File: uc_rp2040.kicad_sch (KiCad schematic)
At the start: 35 parts

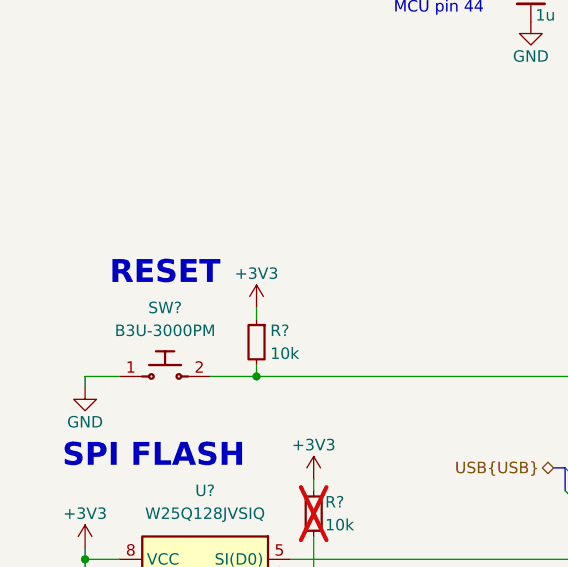
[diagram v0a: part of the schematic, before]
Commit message: [#72133] Add USB mux
Signed-off-by: Dawid Lentka <dlentka@antmicro.com>
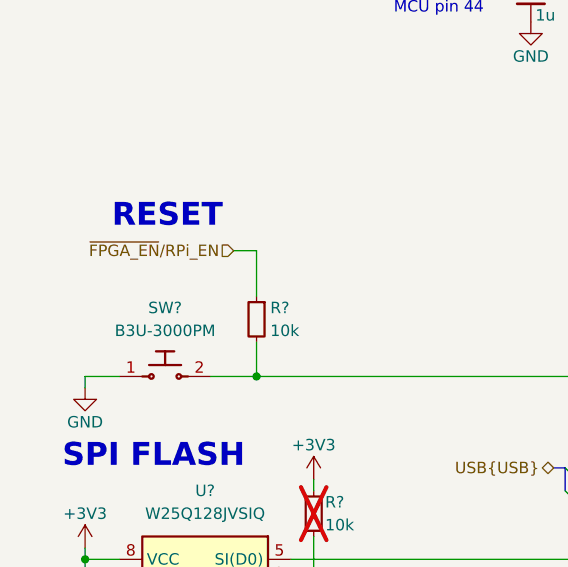
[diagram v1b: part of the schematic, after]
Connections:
- net +3V3: no longer R?.1
- new net ~{FPGA_EN}/RPi_EN: R?.1
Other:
- moved on the sheet: R?
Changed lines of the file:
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@@
 	(wire
 		(pts
-			(xy 91.44 95.25) (xy 91.44 96.52)
+			(xy 91.44 92.71) (xy 91.44 96.52)
 		)
 		(stroke
@@
 	(wire
 		(pts
+			(xy 88.9 82.55) (xy 91.44 82.55)
+		)
+		(stroke
+			(width 0)
+			(type default)
+		)
+	)
+	(wire
+		(pts
 			(xy 121.92 50.8) (xy 128.27 50.8)
 		)
@@
 	(wire
 		(pts
-			(xy 91.44 88.9) (xy 91.44 90.17)
-		)
-		(stroke
-			(width 0)
-			(type default)
-		)
-	)
-	(wire
-		(pts
 			(xy 199.39 144.78) (xy 231.14 144.78)
 		)
@@
 	(wire
 		(pts
+			(xy 91.44 82.55) (xy 91.44 87.63)
+		)
+		(stroke
+			(width 0)
+			(type default)
+		)
+	)
+	(wire
+		(pts
 			(xy 99.06 129.54) (xy 99.06 134.62)
 		)
@@
 	(text "RESET"
 		(exclude_from_sim no)
-		(at 81.28 85.09 0)
+		(at 81.534 78.74 0)
 		(effects
 			(font
@@
 		)
 	)
+	(hierarchical_label "~{FPGA_EN}{slash}RPi_EN"
+		(shape input)
+		(at 88.9 82.55 180)
+		(fields_autoplaced yes)
+		(effects
+			(font
+				(size 1.27 1.27)
+			)
+			(justify right)
+		)
+	)
 	(hierarchical_label "Trig{Triggers}"
 		(shape input)
@@
 	(symbol
 		(lib_id "antmicroResistors0402:R_10k_0402")
-		(at 91.44 90.17 270)
+		(at 91.44 87.63 270)
 		(unit 1)
 		(exclude_from_sim no)
@@
 		(dnp no)
 		(property "Reference" "R?"
-			(at 92.964 91.44 90)
+			(at 92.964 88.9 90)
 			(effects
 				(font
@@
 		)
 		(property "Value" "R_10k_0402"
-			(at 78.74 110.49 0)
+			(at 78.74 107.95 0)
 			(effects
 				(font
@@
 		)
 		(property "Footprint" "antmicro-footprints:R_0402_1005Metric"
-			(at 76.2 110.49 0)
+			(at 76.2 107.95 0)
 			(effects
 				(font
@@
 		)
 		(property "Datasheet" "https://www.bourns.com/docs/product-datasheets/cr.pdf"
-			(at 73.66 110.49 0)
+			(at 73.66 107.95 0)
 			(effects
 				(font
@@
 		)
 		(property "Description" "SMD Chip Resistor, 10 kohm, ± 1%, 62.5 mW, 0402 [1005 Metric], Thick Film, General Purpose"
-			(at 91.44 90.17 0)
+			(at 91.44 87.63 0)
 			(effects
 				(font
@@
 		)
 		(property "MPN" "CR0402-FX-1002GLF"
-			(at 71.12 110.49 0)
+			(at 71.12 107.95 0)
 			(effects
 				(font
@@
 		)
 		(property "Manufacturer" "Bourns"
-			(at 68.58 110.49 0)
+			(at 68.58 107.95 0)
 			(effects
 				(font
@@
 		)
 		(property "License" "Apache-2.0"
-			(at 66.04 110.49 0)
+			(at 66.04 107.95 0)
 			(effects
 				(font
@@
 		)
 		(property "Author" "Antmicro"
-			(at 63.5 110.49 0)
+			(at 63.5 107.95 0)
 			(effects
 				(font
@@
 		)
 		(property "Val" "10k"
-			(at 92.964 93.98 90)
+			(at 92.964 91.44 90)
 			(effects
 				(font
@@
 		)
 		(property "Tolerance" "1%"
-			(at 81.28 110.49 0)
+			(at 81.28 107.95 0)
 			(effects
 				(font
@@
 					(unit 1)
 				)
-			)
-		)
-	)
-	(symbol
-		(lib_id "antmicropower:+3V3")
-		(at 91.44 88.9 0)
-		(unit 1)
-		(exclude_from_sim no)
-		(in_bom yes)
-		(on_board yes)
-		(dnp no)
-		(property "Reference" "#PWR057"
-			(at 106.68 88.9 0)
-			(effects
-				(font
-					(size 1.27 1.27)
-					(thickness 0.15)
-				)
-				(justify left bottom)
-				(hide yes)
-			)
-		)
-		(property "Value" "+3V3"
-			(at 91.44 85.09 0)
-			(effects
-				(font
-					(size 1.27 1.27)
-					(thickness 0.15)
-				)
-			)
-		)
-		(property "Footprint" ""
-			(at 106.68 96.52 0)
-			(effects
-				(font
-					(size 1.27 1.27)
-					(thickness 0.15)
-				)
-				(justify left bottom)
-				(hide yes)
-			)
-		)
-		(property "Datasheet" ""
-			(at 106.68 99.06 0)
-			(effects
-				(font
-					(size 1.27 1.27)
-					(thickness 0.15)
-				)
-				(justify left bottom)
-				(hide yes)
-			)
-		)
-		(property "Description" ""
-			(at 91.44 88.9 0)
-			(effects
-				(font
-					(size 1.27 1.27)
-				)
-				(hide yes)
-			)
-		)
-		(property "Author" "Antmicro"
-			(at 106.68 91.44 0)
-			(effects
-				(font
-					(size 1.27 1.27)
-					(thickness 0.15)
-				)
-				(justify left bottom)
-				(hide yes)
-			)
-		)
-		(property "License" "Apache-2.0"
-			(at 106.68 93.98 0)
-			(effects
-				(font
-					(size 1.27 1.27)
-					(thickness 0.15)
-				)
-				(justify left bottom)
-				(hide yes)
-			)
-		)
-		(pin "1"
-		)
-		(instances
-			(project "led-panel"
-				(path "/a86e1cab-ea0a-45e6-9194-d44b0d5c9450/06971436-f55c-4c9a-b2a5-5e1b832e9517"
-					(reference "#PWR057")
-					(unit 1)
-				)

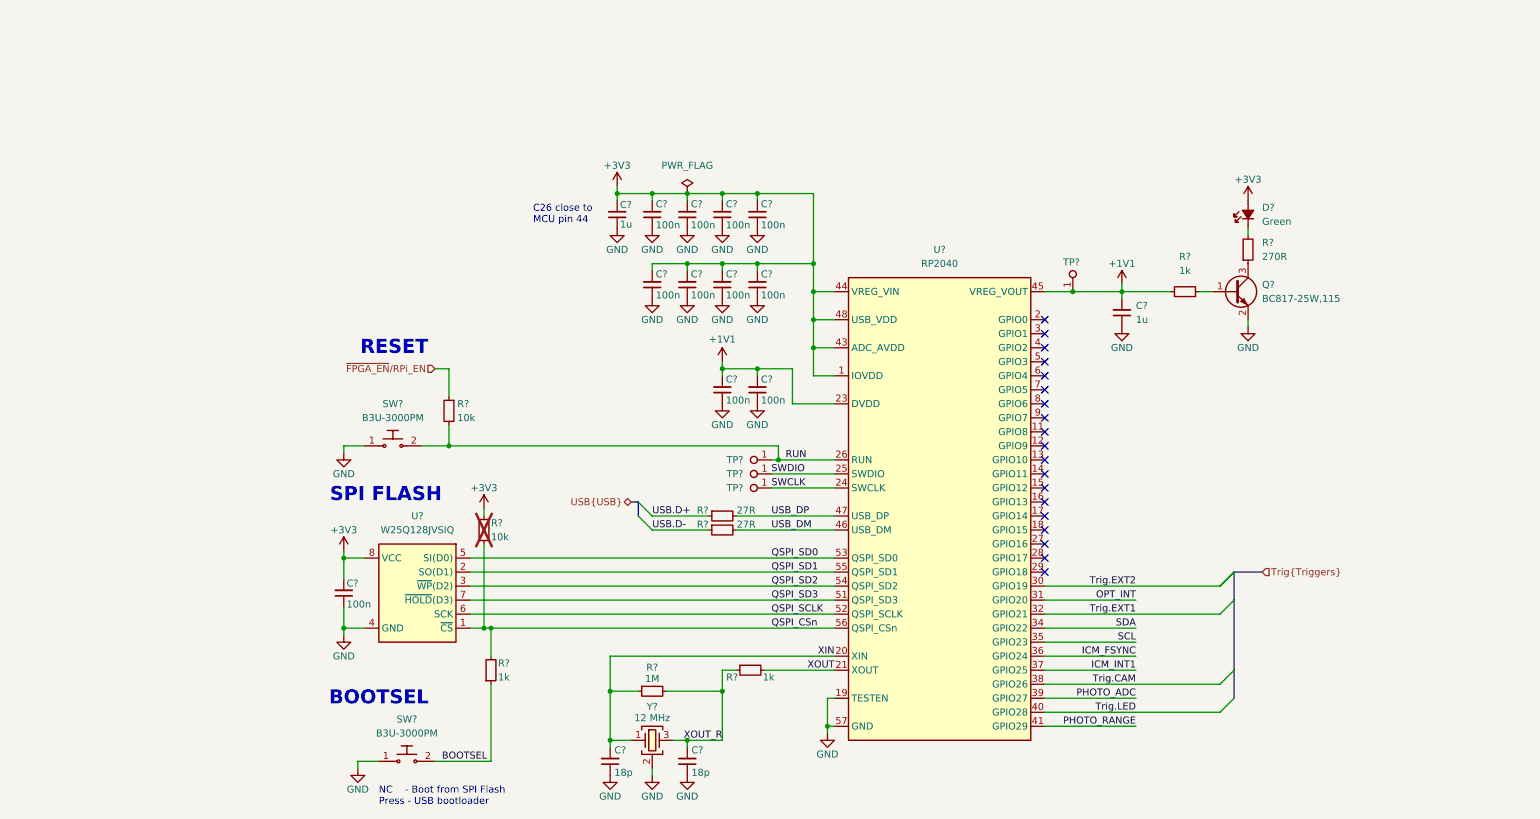
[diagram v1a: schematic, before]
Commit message: [#72133] Move executor switching to new scheet; Add FPGA flash programmer
Signed-off-by: Dawid Lentka <dlentka@antmicro.com>
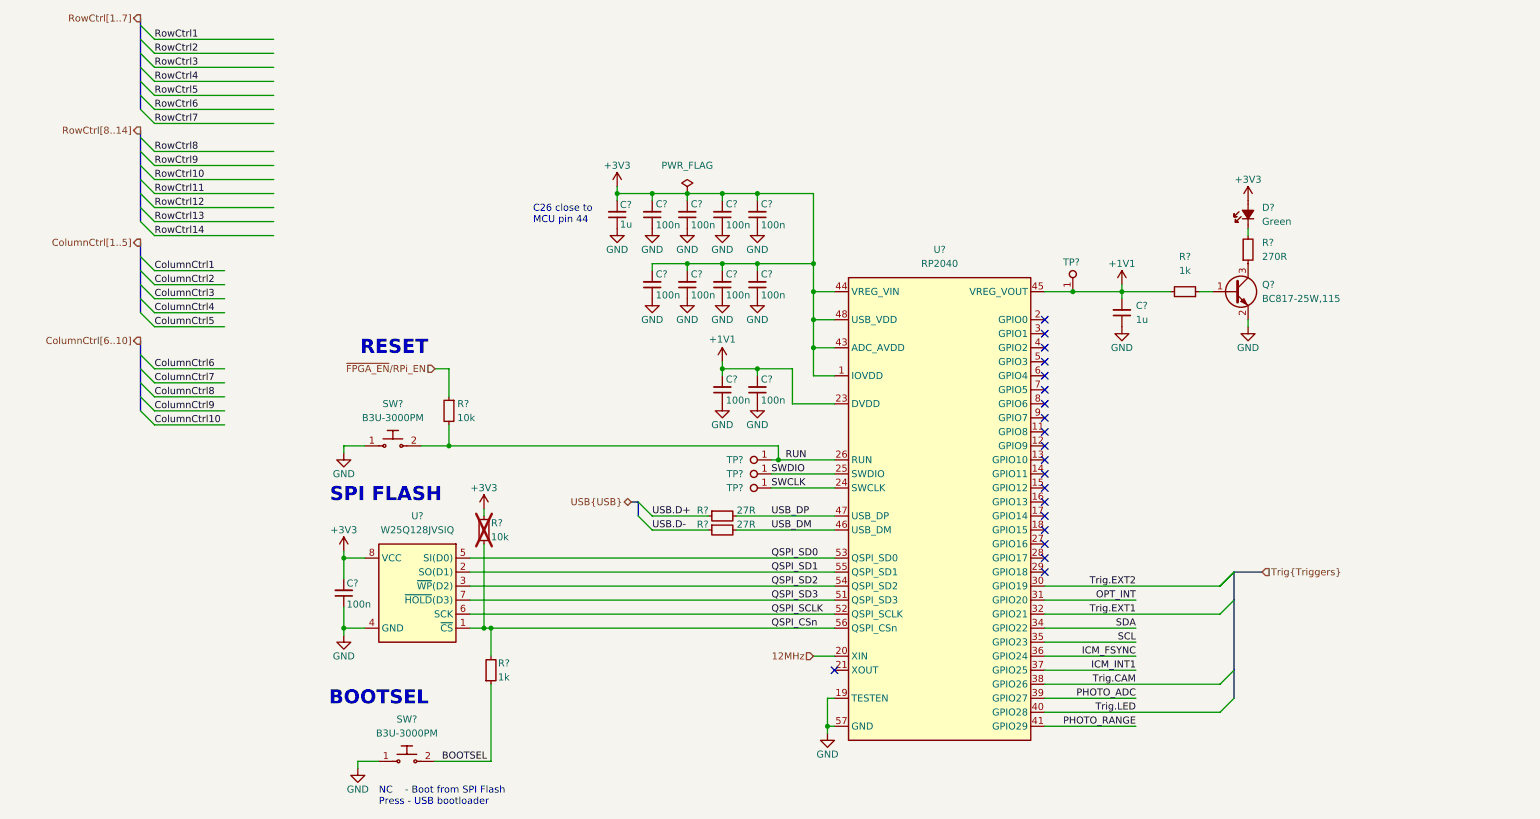
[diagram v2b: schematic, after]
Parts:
- removed C? (x2): C_18p_0402, antmicro-footprints:C_0402_1005Metric, symbol antmicroCapacitors0402:C_18p_0402
- removed R?: R_1k_0402, antmicro-footprints:R_0402_1005Metric, symbol antmicroResistors0402:R_1k_0402
- removed R?: R_1M_0402, antmicro-footprints:R_0402_1005Metric, symbol antmicroResistors0402:R_1M_0402
- removed Y?: Resonator_12MHz_ABM8G, antmicro-footprints:Resonator_SMD_Abracon_ABM8G_3.2x2.5mm, symbol antmicroResonators:Resonator_12MHz_ABM8G
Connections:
- net XIN renamed 12MHz
- net XOUT: no longer names the net of U?.21 (XOUT)
- no-connect marks 19 -> 20

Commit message: [#72133] Unify sheet size
Signed-off-by: Dawid Lentka <dlentka@antmicro.com>
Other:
- title: (none) -> LED Panel Board
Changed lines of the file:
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@@
 	(generator_version "8.0")
 	(paper "A4")
+	(title_block
+		(title "LED Panel Board")
+		(date "28.01.2025")
+		(rev "1.0.0")
+	)
 	(bus_alias "LEDCtrl"
 		(members "Row[1..14]" "Column[1..7]")

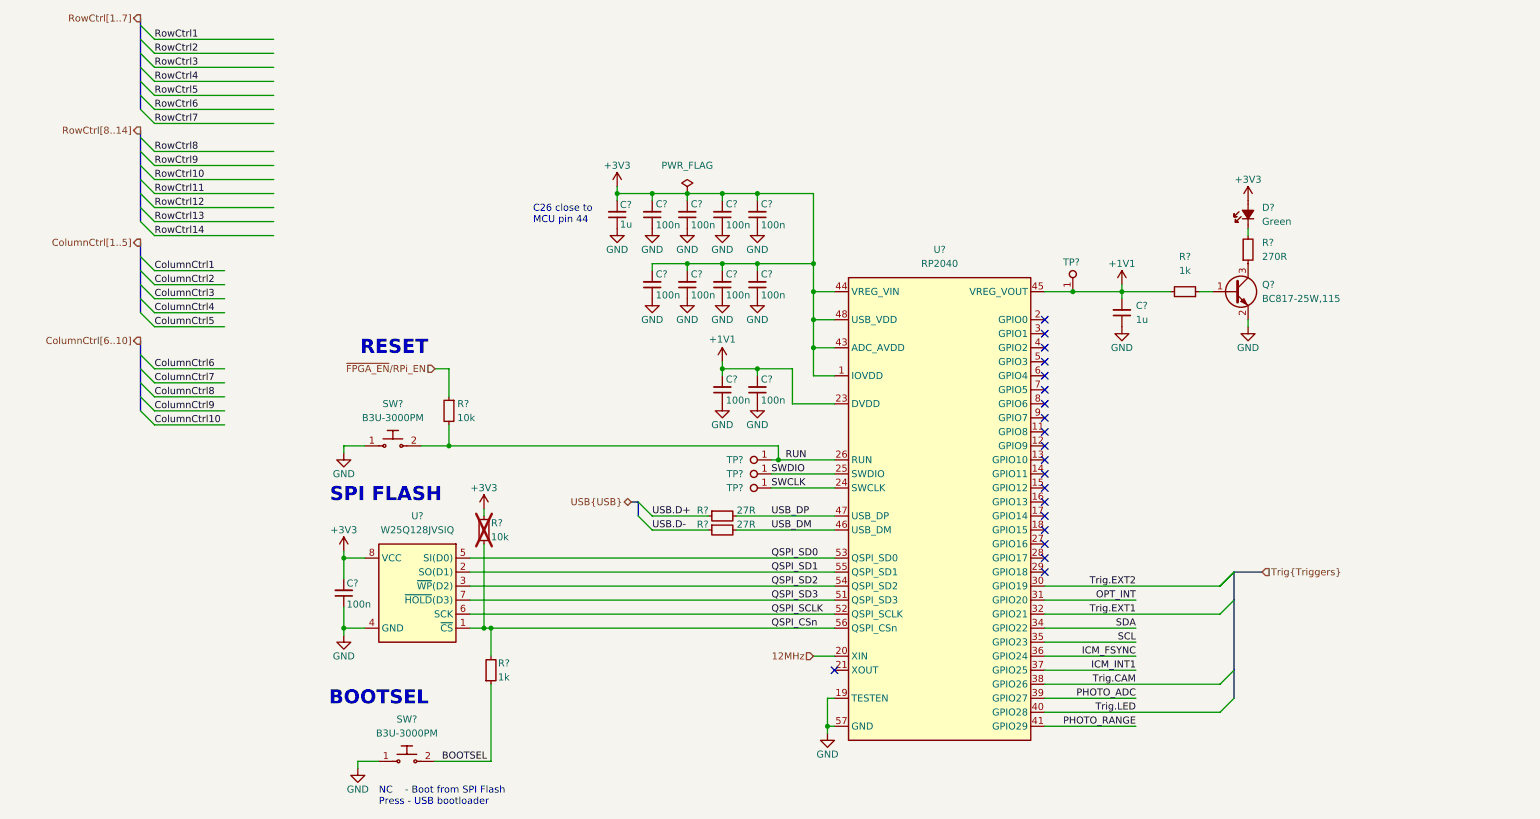
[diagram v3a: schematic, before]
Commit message: [#72133] Add indicator LEDs & testpoints
Signed-off-by: Dawid Lentka <dlentka@antmicro.com>
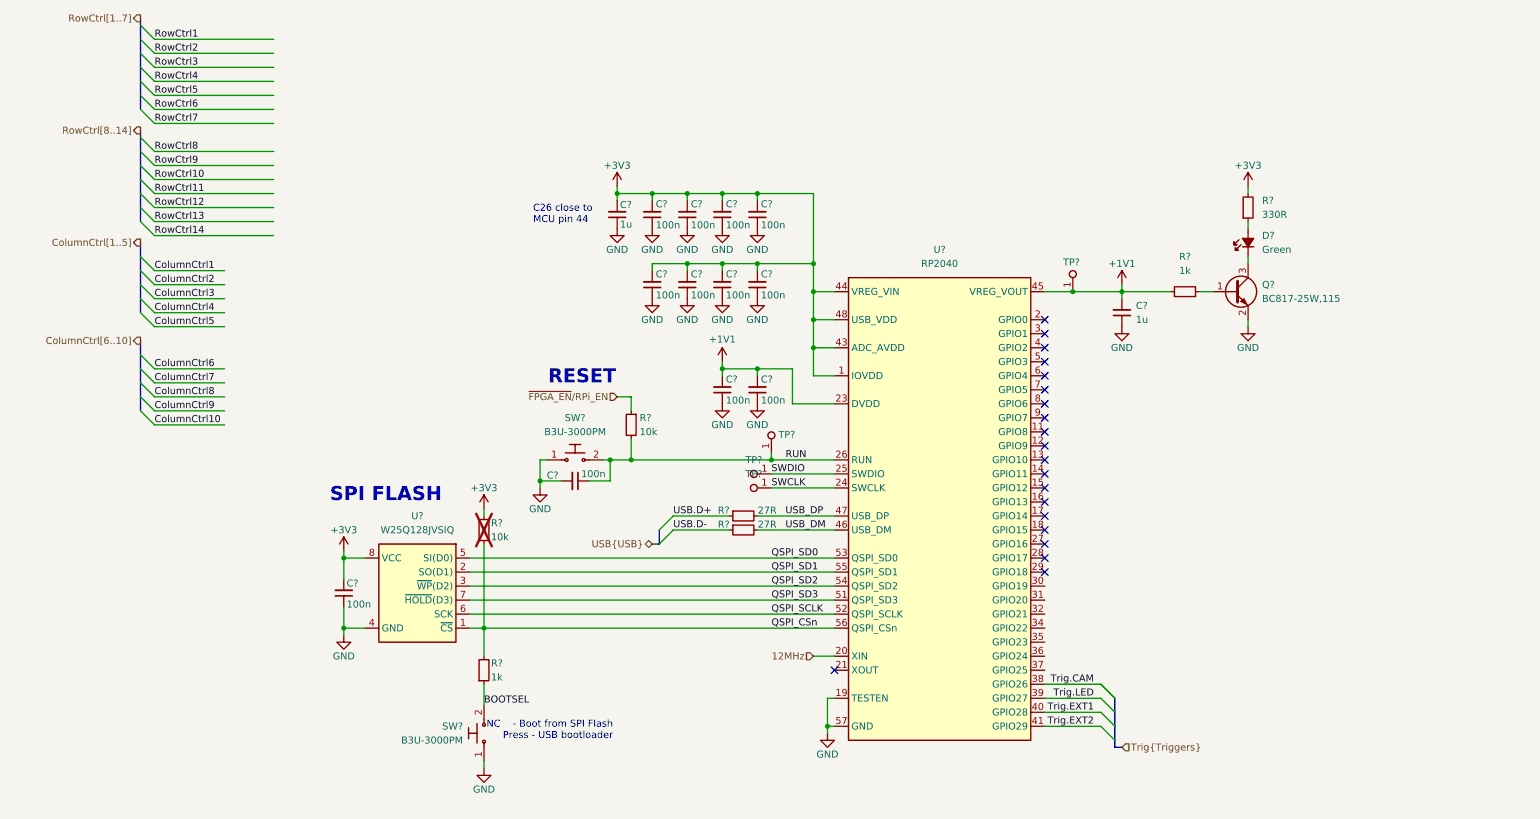
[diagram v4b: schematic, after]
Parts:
- removed D?: LED_G_0402_VLMTG1500-GS08, antmicro-footprints:LED_0402_1005Metric_G, symbol antmicroLEDIndicationDiscrete:LED_G_0402_VLMTG1500-GS08
- removed R?: R_270R_0402, antmicro-footprints:R_0402_1005Metric, symbol antmicroResistors0402:R_270R_0402
- added C?: C_100n_16V_X7R_0402, antmicro-footprints:C_0402_1005Metric, symbol antmicroCapacitors0402:C_100n_16V_X7R_0402
- added D?: LED_G_0603_KP-1608CGCK, antmicro-footprints:LED_0603_1608Metric_G, symbol antmicroLEDIndicationDiscrete:LED_G_0603_KP-1608CGCK
- added R?: R_330R_0402, antmicro-footprints:R_0402_1005Metric, symbol antmicroResistors0402:R_330R_0402
- TP? (x4): value TP_1mm_SMD -> TP_0.75mm_SMD; footprint antmicro-footprints:TP_SMD_1mm -> antmicro-footprints:TP_SMD_0.75mm; symbol antmicroTestPoints:TP_1mm_SMD -> antmicroTestPoints:TP_0.75mm_SMD
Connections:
- net PHOTO_ADC is gone; now on net Trig.LED: U?.39 (GPIO27)
- net PHOTO_RANGE is gone; now on net Trig.EXT2: U?.41 (GPIO29)
- net +3V3: now also R?.2
- net GND: now also C?.2
- net RUN: now also C?.1
- net Trig.EXT1: now also U?.40 (GPIO28); no longer U?.32 (GPIO21)
- net Trig.EXT2: no longer U?.30 (GPIO19)
- net Trig.LED: no longer U?.40 (GPIO28)
- net at Q?.3 (C): now also D?.1 (C)
- net ICM_FSYNC: no longer names the net of U?.36 (GPIO24)
- net ICM_INT1: no longer names the net of U?.37 (GPIO25)
- net OPT_INT: no longer names the net of U?.31 (GPIO20)
- net SCL: no longer names the net of U?.35 (GPIO23)
- net SDA: no longer names the net of U?.34 (GPIO22)
- new net: D?.2 (A), R?.1
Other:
- note removed: "BOOTSEL"
- moved on the sheet: R?, SW?, TP?

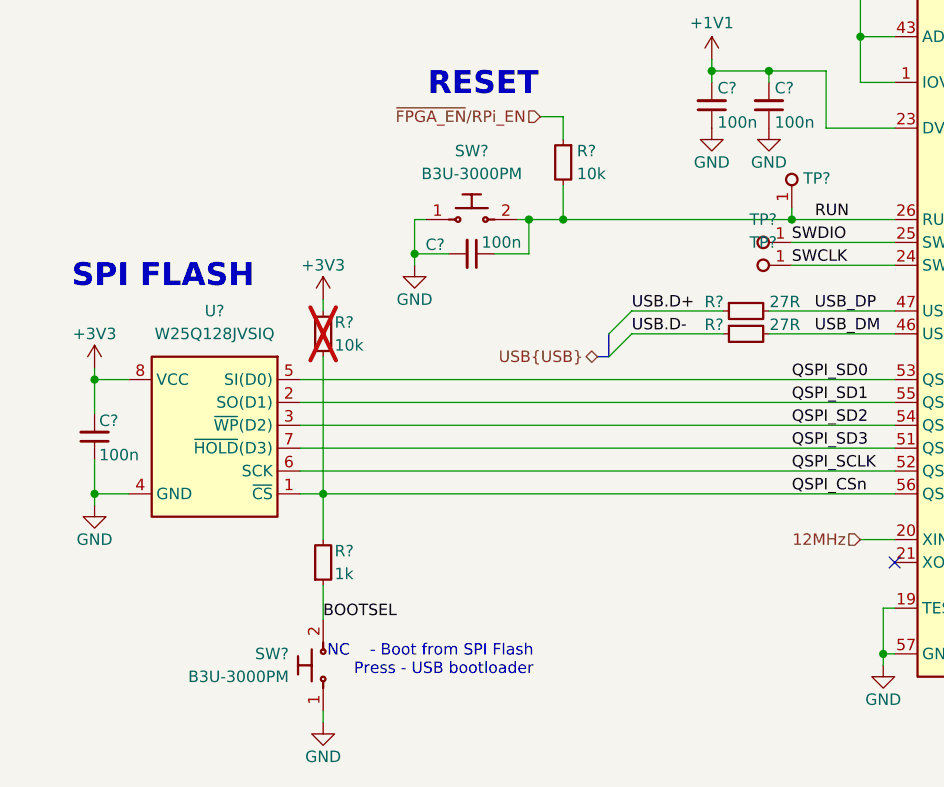
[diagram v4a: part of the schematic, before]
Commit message: [#72133] Unify components
Signed-off-by: Dawid Lentka <dlentka@antmicro.com>
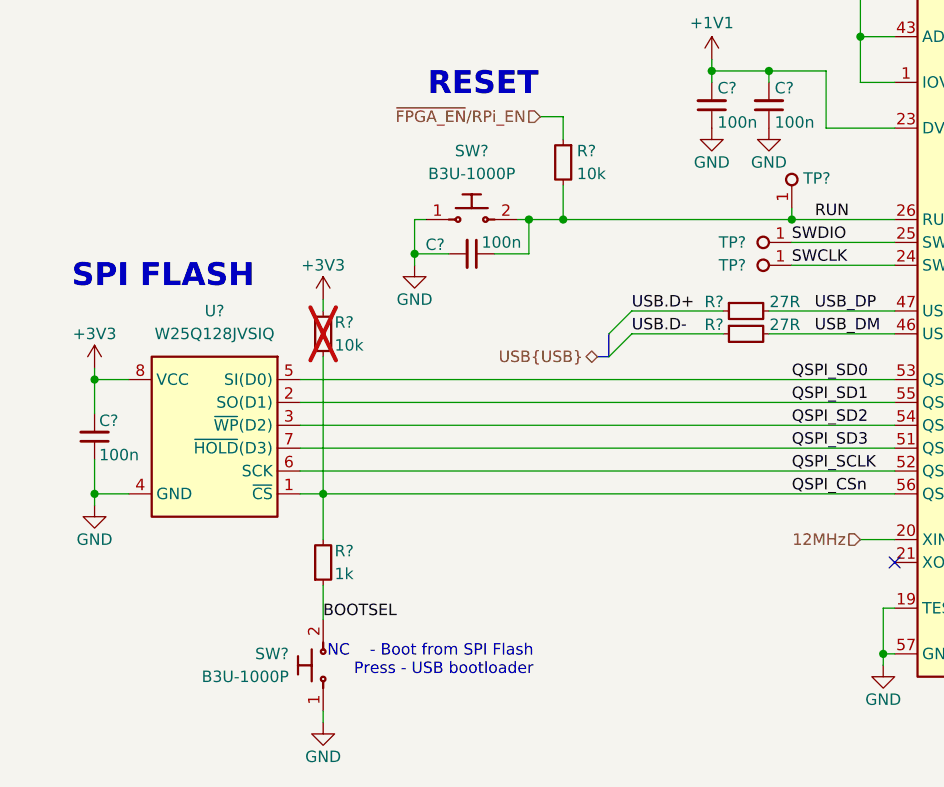
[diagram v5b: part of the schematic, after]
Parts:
- removed SW? (x2): SW_B3U-3000PM_SMD, antmicro-footprints:SW_B3U-3000PM_SMD, symbol antmicroPushbuttonSwitches:SW_B3U-3000PM_SMD
- added SW? (x2): SW_B3U-1000P_SMD, antmicro-footprints:SW_B3U-1000P_SMD, symbol antmicroPushbuttonSwitches:SW_B3U-1000P_SMD
- C? (x11): value C_100n_16V_X7R_0402 -> C_100n_0402; symbol antmicroCapacitors0402:C_100n_16V_X7R_0402 -> antmicroCapacitors0402:C_100n_0402; Dielectric X7R -> X5R; MPN C0402C104J4RAC7411 -> GRM155R61H104KE14D; Manufacturer KEMET -> Murata; Voltage 16V -> 50V
- C? (x2): value C_1u_0402 -> C_1u_16V_0402; symbol antmicroCapacitors0402:C_1u_0402 -> antmicroCapacitors0402:C_1u_16V_0402; MPN C1005X6S1A105K050BC -> C0402C105M4PACTU; Manufacturer TDK -> KEMET; Voltage (none) -> 16V
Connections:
- net BOOTSEL: now also SW?.2
- net GND: now also SW?.1, SW?.1
- net RUN: now also SW?.2
